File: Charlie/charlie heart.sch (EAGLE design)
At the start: 29 parts, among them Q1 BSA223SP

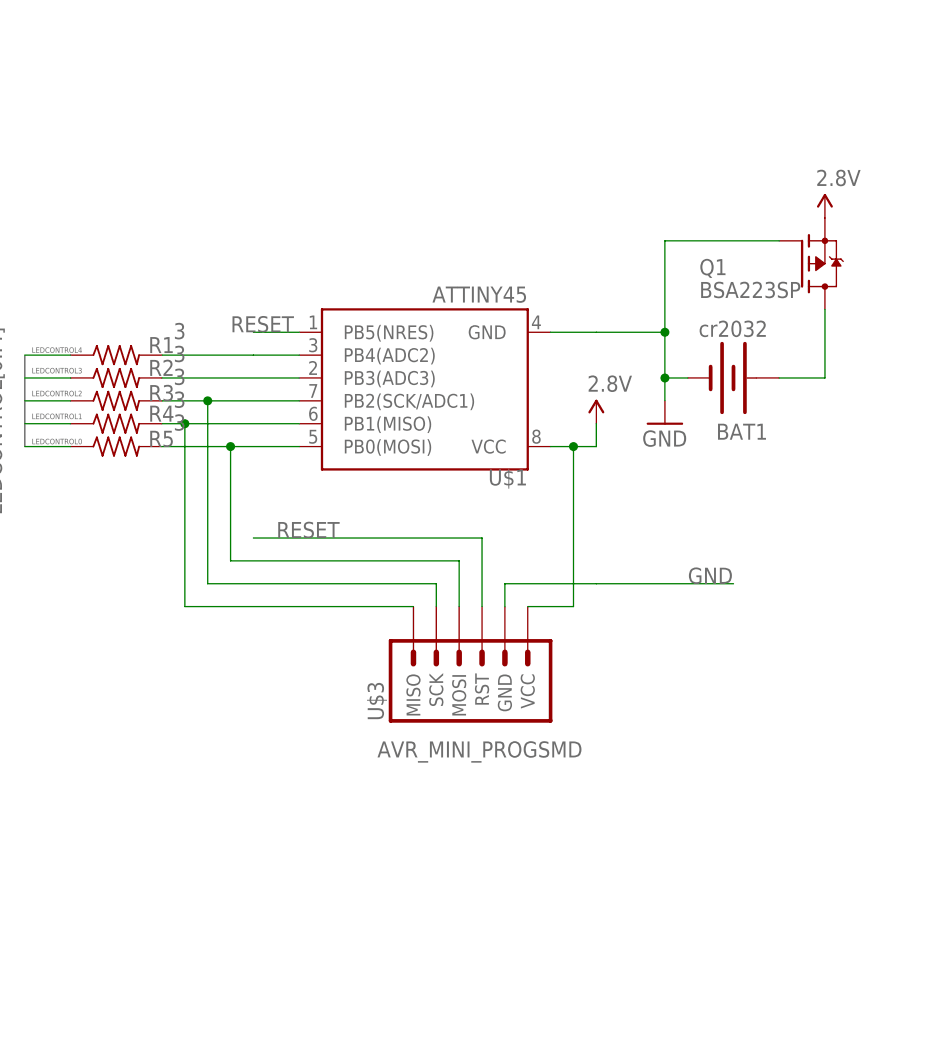
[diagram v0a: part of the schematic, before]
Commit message: add proper board file, and add mosfet for reverse battery safety
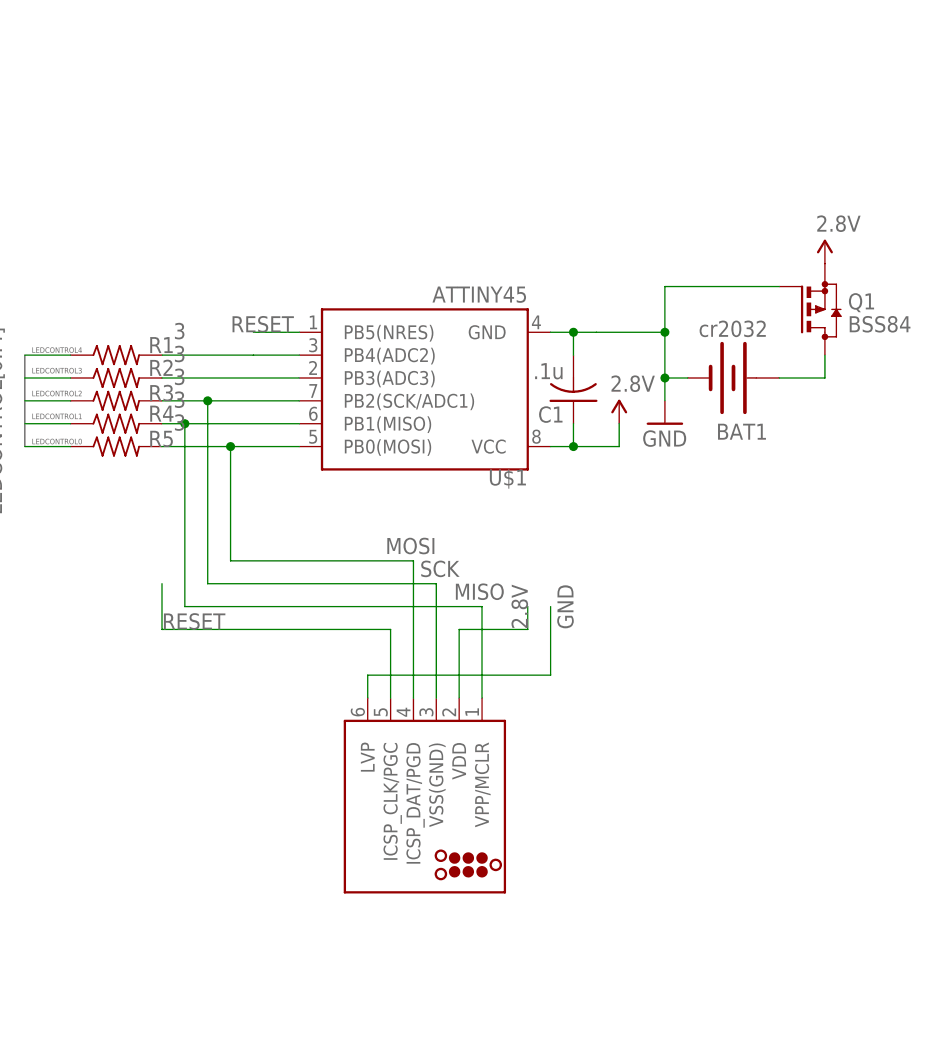
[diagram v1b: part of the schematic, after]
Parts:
- removed U$3: AVR_MINI_PROGSMD, SparkFun:AVR_MINI_PROGSMD
- added C1: .1u, rcl:C-USC1206
- added J1: (no value), tag-connect:TC2030-MCP-NL
- Q1: value BSA223SP -> BSS84; device transistor-fet:BSA223SP -> transistor-small-signal:BSS84
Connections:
- removed net N$1: R5.2, U$1.PB0(MOSI), U$3.MOSI
- removed net N$3: R3.2, U$1.PB2(SCK/ADC1), U$3.SCK
- removed net N$7: BAT1.+
- new net MISO: J1.VPP/MCLR, R4.2, U$1.PB1(MISO)
- new net MOSI: J1.ICSP_DAT/PGD, R5.2, U$1.PB0(MOSI)
- new net SCK: J1.VSS(GND), R3.2, U$1.PB2(SCK/ADC1)
- net 2.8V: now also C1.1, J1.VDD; no longer U$3.VCC
- net GND: now also C1.2, J1.LVP; no longer U$3.GND
- net N$2: now also BAT1.+, Q1.D; no longer R4.2, U$1.PB1(MISO), U$3.MISO
- net RESET: now also J1.ICSP_CLK/PGC; no longer U$3.RST
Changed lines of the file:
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@@
 <part name="BAT1" library="SparkFun" deviceset="BATTERY" device="20SMD" value="cr2032"/>
 <part name="GND1" library="SparkFun" deviceset="GND" device=""/>
-<part name="U$3" library="SparkFun" deviceset="AVR_MINI_PROG" device="SMD"/>
-<part name="Q1" library="transistor-fet" deviceset="BSA223SP" device=""/>
+<part name="C1" library="rcl" deviceset="C-US" device="C1206" value=".1u"/>
+<part name="J1" library="tag-connect" deviceset="TC2030" device="-MCP-NL"/>
+<part name="Q1" library="transistor-small-signal" deviceset="BSS84" device=""/>
 <part name="SUPPLY1" library="SparkFun-Aesthetics" deviceset="2.8V" device=""/>
 <part name="SUPPLY2" library="SparkFun-Aesthetics" deviceset="2.8V" device=""/>
@@
 <instance part="BAT1" gate="G$1" x="261.62" y="53.34" rot="R180"/>
 <instance part="GND1" gate="1" x="254" y="48.26"/>
-<instance part="U$3" gate="G$1" x="233.68" y="20.32" smashed="yes" rot="R270">
-<attribute name="NAME" x="222.758" y="15.24" size="1.778" layer="95" rot="R90"/>
-<attribute name="VALUE" x="244.856" y="12.954" size="1.778" layer="96" rot="R180"/>
-</instance>
-<instance part="Q1" gate="G$1" x="269.24" y="66.04"/>
-<instance part="SUPPLY1" gate="G$1" x="271.78" y="71.12"/>
-<instance part="SUPPLY2" gate="G$1" x="246.38" y="48.26"/>
+<instance part="C1" gate="G$1" x="243.84" y="50.8" rot="R180"/>
+<instance part="J1" gate="G$1" x="226.06" y="5.08" rot="R270"/>
+<instance part="Q1" gate="G$1" x="271.78" y="60.96"/>
+<instance part="SUPPLY1" gate="G$1" x="271.78" y="66.04"/>
+<instance part="SUPPLY2" gate="G$1" x="248.92" y="48.26"/>
 </instances>
 <busses>
@@
 </segment>
 </net>
-<net name="N$1" class="0">
+<net name="MOSI" class="0">
 <segment>
 <wire x1="213.36" y1="45.72" x2="205.74" y2="45.72" width="0.1524" layer="91"/>
 <wire x1="205.74" y1="45.72" x2="198.12" y2="45.72" width="0.1524" layer="91"/>
-<wire x1="231.14" y1="27.94" x2="231.14" y2="33.02" width="0.1524" layer="91"/>
-<wire x1="231.14" y1="33.02" x2="205.74" y2="33.02" width="0.1524" layer="91"/>
 <wire x1="205.74" y1="33.02" x2="205.74" y2="45.72" width="0.1524" layer="91"/>
 <junction x="205.74" y="45.72"/>
 <pinref part="U$1" gate="G$1" pin="PB0(MOSI)"/>
 <pinref part="R5" gate="G$1" pin="2"/>
-<pinref part="U$3" gate="G$1" pin="MOSI"/>
-</segment>
-</net>
-<net name="N$2" class="0">
+<pinref part="J1" gate="G$1" pin="ICSP_DAT/PGD"/>
+<wire x1="226.06" y1="17.78" x2="226.06" y2="33.02" width="0.1524" layer="91"/>
+<wire x1="226.06" y1="33.02" x2="205.74" y2="33.02" width="0.1524" layer="91"/>
+<label x="228.6" y="35.56" size="1.778" layer="95" rot="R180"/>
+</segment>
+</net>
+<net name="MISO" class="0">
 <segment>
 <wire x1="213.36" y1="48.26" x2="200.66" y2="48.26" width="0.1524" layer="91"/>
 <wire x1="200.66" y1="48.26" x2="198.12" y2="48.26" width="0.1524" layer="91"/>
-<wire x1="226.06" y1="27.94" x2="200.66" y2="27.94" width="0.1524" layer="91"/>
 <wire x1="200.66" y1="27.94" x2="200.66" y2="48.26" width="0.1524" layer="91"/>
 <junction x="200.66" y="48.26"/>
 <pinref part="U$1" gate="G$1" pin="PB1(MISO)"/>
 <pinref part="R4" gate="G$1" pin="2"/>
-<pinref part="U$3" gate="G$1" pin="MISO"/>
-</segment>
-</net>
-<net name="N$3" class="0">
+<pinref part="J1" gate="G$1" pin="VPP/MCLR"/>
+<wire x1="233.68" y1="17.78" x2="233.68" y2="27.94" width="0.1524" layer="91"/>
+<wire x1="233.68" y1="27.94" x2="200.66" y2="27.94" width="0.1524" layer="91"/>
+<label x="236.22" y="30.48" size="1.778" layer="95" rot="R180"/>
+</segment>
+</net>
+<net name="SCK" class="0">
 <segment>
 <wire x1="213.36" y1="50.8" x2="203.2" y2="50.8" width="0.1524" layer="91"/>
 <wire x1="203.2" y1="50.8" x2="198.12" y2="50.8" width="0.1524" layer="91"/>
-<wire x1="228.6" y1="27.94" x2="228.6" y2="30.48" width="0.1524" layer="91"/>
-<wire x1="228.6" y1="30.48" x2="203.2" y2="30.48" width="0.1524" layer="91"/>
 <wire x1="203.2" y1="30.48" x2="203.2" y2="50.8" width="0.1524" layer="91"/>
 <junction x="203.2" y="50.8"/>
 <pinref part="U$1" gate="G$1" pin="PB2(SCK/ADC1)"/>
 <pinref part="R3" gate="G$1" pin="2"/>
-<pinref part="U$3" gate="G$1" pin="SCK"/>
+<pinref part="J1" gate="G$1" pin="VSS(GND)"/>
+<wire x1="228.6" y1="17.78" x2="228.6" y2="30.48" width="0.1524" layer="91"/>
+<wire x1="228.6" y1="30.48" x2="203.2" y2="30.48" width="0.1524" layer="91"/>
+<label x="231.14" y="33.02" size="1.778" layer="95" rot="R180"/>
 </segment>
 </net>
@@
 <wire x1="256.54" y1="53.34" x2="254" y2="53.34" width="0.1524" layer="91"/>
 <wire x1="254" y1="53.34" x2="254" y2="50.8" width="0.1524" layer="91"/>
-<wire x1="241.3" y1="58.42" x2="246.38" y2="58.42" width="0.1524" layer="91"/>
+<wire x1="241.3" y1="58.42" x2="243.84" y2="58.42" width="0.1524" layer="91"/>
+<wire x1="243.84" y1="58.42" x2="246.38" y2="58.42" width="0.1524" layer="91"/>
 <wire x1="246.38" y1="58.42" x2="254" y2="58.42" width="0.1524" layer="91"/>
 <wire x1="254" y1="58.42" x2="254" y2="53.34" width="0.1524" layer="91"/>
@@
 <pinref part="GND1" gate="1" pin="GND"/>
 <pinref part="U$1" gate="G$1" pin="GND"/>
+<pinref part="C1" gate="G$1" pin="2"/>
+<wire x1="243.84" y1="55.88" x2="243.84" y2="58.42" width="0.1524" layer="91"/>
+<junction x="243.84" y="58.42"/>
 <pinref part="Q1" gate="G$1" pin="G"/>
-<wire x1="266.7" y1="68.58" x2="254" y2="68.58" width="0.1524" layer="91"/>
-<wire x1="254" y1="68.58" x2="254" y2="58.42" width="0.1524" layer="91"/>
+<wire x1="266.7" y1="63.5" x2="254" y2="63.5" width="0.1524" layer="91"/>
+<wire x1="254" y1="63.5" x2="254" y2="58.42" width="0.1524" layer="91"/>
 <junction x="254" y="58.42"/>
 </segment>
 <segment>
-<wire x1="261.62" y1="30.48" x2="246.38" y2="30.48" width="0.1524" layer="91"/>
-<wire x1="246.38" y1="30.48" x2="236.22" y2="30.48" width="0.1524" layer="91"/>
-<wire x1="236.22" y1="30.48" x2="236.22" y2="27.94" width="0.1524" layer="91"/>
-<pinref part="U$3" gate="G$1" pin="GND"/>
-<label x="256.54" y="30.48" size="1.778" layer="95"/>
+<pinref part="J1" gate="G$1" pin="LVP"/>
+<wire x1="220.98" y1="17.78" x2="220.98" y2="20.32" width="0.1524" layer="91"/>
+<wire x1="220.98" y1="20.32" x2="241.3" y2="20.32" width="0.1524" layer="91"/>
+<wire x1="241.3" y1="20.32" x2="241.3" y2="27.94" width="0.1524" layer="91"/>
+<label x="243.84" y="25.4" size="1.778" layer="95" rot="R90"/>
+</segment>
+</net>
+<net name="2.8V" class="0">
+<segment>
+<pinref part="J1" gate="G$1" pin="VDD"/>
+<wire x1="231.14" y1="17.78" x2="231.14" y2="25.4" width="0.1524" layer="91"/>
+<wire x1="231.14" y1="25.4" x2="238.76" y2="25.4" width="0.1524" layer="91"/>
+<wire x1="238.76" y1="25.4" x2="238.76" y2="27.94" width="0.1524" layer="91"/>
+<label x="238.76" y="25.4" size="1.778" layer="95" rot="R90"/>
+</segment>
+<segment>
+<pinref part="Q1" gate="G$1" pin="S"/>
+<pinref part="SUPPLY1" gate="G$1" pin="2.8V"/>
+</segment>
+<segment>
+<pinref part="C1" gate="G$1" pin="1"/>
+<wire x1="243.84" y1="48.26" x2="243.84" y2="45.72" width="0.1524" layer="91"/>
+<wire x1="241.3" y1="45.72" x2="243.84" y2="45.72" width="0.1524" layer="91"/>
+<pinref part="U$1" gate="G$1" pin="VCC"/>
+<wire x1="243.84" y1="45.72" x2="248.92" y2="45.72" width="0.1524" layer="91"/>
+<wire x1="248.92" y1="45.72" x2="248.92" y2="48.26" width="0.1524" layer="91"/>
+<junction x="243.84" y="45.72"/>
+<pinref part="SUPPLY2" gate="G$1" pin="2.8V"/>
 </segment>
 </net>
@@
 </segment>
 <segment>
-<wire x1="233.68" y1="35.56" x2="208.28" y2="35.56" width="0.1524" layer="91"/>
-<wire x1="233.68" y1="27.94" x2="233.68" y2="35.56" width="0.1524" layer="91"/>
-<label x="210.82" y="35.56" size="1.778" layer="95"/>
-<pinref part="U$3" gate="G$1" pin="RST"/>
-</segment>
-</net>
-<net name="N$7" class="0">
-<segment>
-<wire x1="271.78" y1="53.34" x2="271.78" y2="60.96" width="0.1524" layer="91"/>
+<pinref part="J1" gate="G$1" pin="ICSP_CLK/PGC"/>
+<wire x1="223.52" y1="17.78" x2="223.52" y2="25.4" width="0.1524" layer="91"/>
+<wire x1="223.52" y1="25.4" x2="198.12" y2="25.4" width="0.1524" layer="91"/>
+<wire x1="198.12" y1="25.4" x2="198.12" y2="30.48" width="0.1524" layer="91"/>
+<label x="198.12" y="25.4" size="1.778" layer="95"/>
+</segment>
+</net>
+<net name="N$2" class="0">
+<segment>
 <wire x1="266.7" y1="53.34" x2="271.78" y2="53.34" width="0.1524" layer="91"/>
 <pinref part="BAT1" gate="G$1" pin="+"/>
-</segment>
-</net>
-<net name="2.8V" class="0">
-<segment>
-<pinref part="Q1" gate="G$1" pin="S"/>
-<pinref part="SUPPLY1" gate="G$1" pin="2.8V"/>
-</segment>
-<segment>
-<wire x1="241.3" y1="45.72" x2="243.84" y2="45.72" width="0.1524" layer="91"/>
-<wire x1="243.84" y1="45.72" x2="243.84" y2="27.94" width="0.1524" layer="91"/>
-<wire x1="243.84" y1="27.94" x2="238.76" y2="27.94" width="0.1524" layer="91"/>
-<pinref part="U$1" gate="G$1" pin="VCC"/>
-<pinref part="U$3" gate="G$1" pin="VCC"/>
-<wire x1="243.84" y1="45.72" x2="246.38" y2="45.72" width="0.1524" layer="91"/>
-<wire x1="246.38" y1="45.72" x2="246.38" y2="48.26" width="0.1524" layer="91"/>
-<junction x="243.84" y="45.72"/>
-<pinref part="SUPPLY2" gate="G$1" pin="2.8V"/>
-</segment>
-</net>
+<pinref part="Q1" gate="G$1" pin="D"/>
+<wire x1="271.78" y1="53.34" x2="271.78" y2="55.88" width="0.1524" layer="91"/>
+</segment>
+</net>

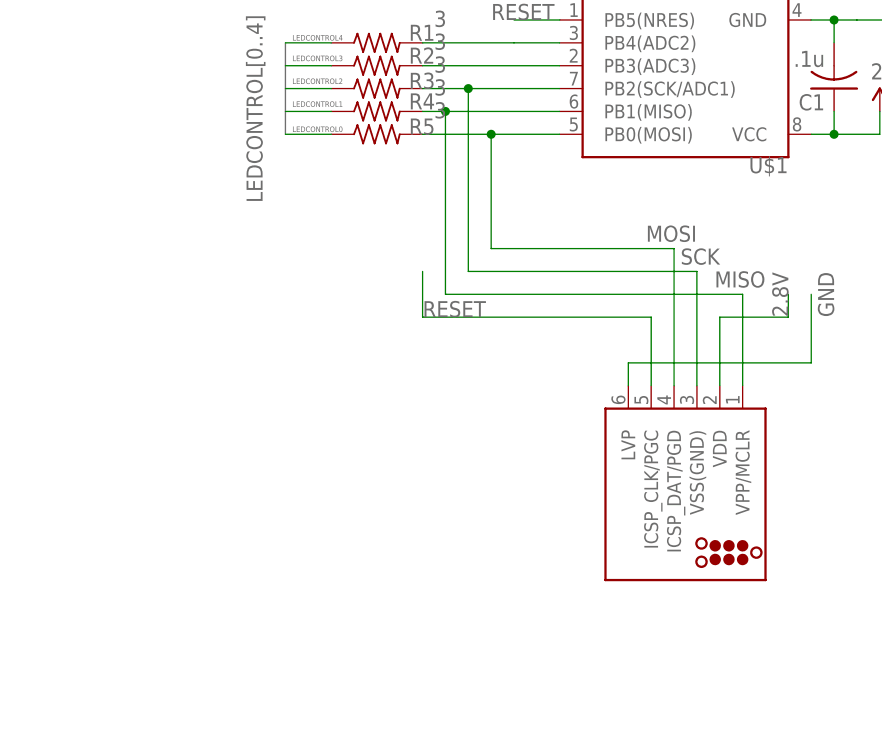
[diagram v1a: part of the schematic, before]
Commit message: add mode switch
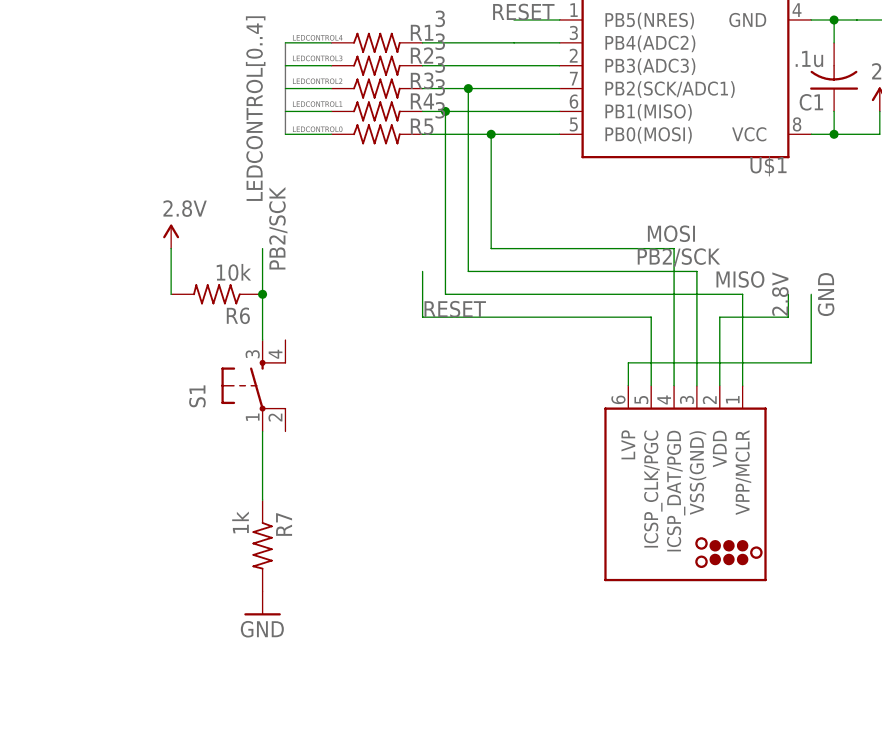
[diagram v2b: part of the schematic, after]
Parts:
- added R6: 10k, rcl:R-US_R0805
- added R7: 1k, rcl:R-US_R0805
- added S1: (no value), SparkFun:TAC_SWITCHSMD
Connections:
- removed net SCK: J1.VSS(GND), R3.2, U$1.PB2(SCK/ADC1)
- new net N$3: R7.1, S1.1
- new net PB2/SCK: J1.VSS(GND), R3.2, R6.1, S1.3, U$1.PB2(SCK/ADC1)
- net 2.8V: now also R6.2
- net GND: now also R7.2
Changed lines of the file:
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@@
 <part name="SUPPLY1" library="SparkFun-Aesthetics" deviceset="2.8V" device=""/>
 <part name="SUPPLY2" library="SparkFun-Aesthetics" deviceset="2.8V" device=""/>
+<part name="S1" library="SparkFun" deviceset="TAC_SWITCH" device="SMD"/>
+<part name="R6" library="rcl" deviceset="R-US_" device="R0805" value="10k"/>
+<part name="R7" library="rcl" deviceset="R-US_" device="R0805" value="1k"/>
+<part name="SUPPLY3" library="SparkFun-Aesthetics" deviceset="2.8V" device=""/>
+<part name="GND2" library="SparkFun-Aesthetics" deviceset="GND" device=""/>
 </parts>
 <sheets>
@@
 <instance part="SUPPLY1" gate="G$1" x="271.78" y="66.04"/>
 <instance part="SUPPLY2" gate="G$1" x="248.92" y="48.26"/>
+<instance part="S1" gate="S" x="180.34" y="17.78" rot="R90"/>
+<instance part="R6" gate="G$1" x="175.26" y="27.94" rot="R180"/>
+<instance part="R7" gate="G$1" x="180.34" y="0" rot="R270"/>
+<instance part="SUPPLY3" gate="G$1" x="170.18" y="33.02"/>
+<instance part="GND2" gate="1" x="180.34" y="-7.62"/>
 </instances>
 <busses>
@@
 </segment>
 </net>
-<net name="SCK" class="0">
+<net name="PB2/SCK" class="0">
 <segment>
 <wire x1="213.36" y1="50.8" x2="203.2" y2="50.8" width="0.1524" layer="91"/>
@@
 <wire x1="228.6" y1="30.48" x2="203.2" y2="30.48" width="0.1524" layer="91"/>
 <label x="231.14" y="33.02" size="1.778" layer="95" rot="R180"/>
+</segment>
+<segment>
+<pinref part="S1" gate="S" pin="3"/>
+<wire x1="180.34" y1="22.86" x2="180.34" y2="27.94" width="0.1524" layer="91"/>
+<pinref part="R6" gate="G$1" pin="1"/>
+<wire x1="180.34" y1="27.94" x2="180.34" y2="33.02" width="0.1524" layer="91"/>
+<junction x="180.34" y="27.94"/>
+<label x="182.88" y="30.48" size="1.778" layer="95" rot="R90"/>
 </segment>
 </net>
@@
 <label x="243.84" y="25.4" size="1.778" layer="95" rot="R90"/>
 </segment>
+<segment>
+<pinref part="R7" gate="G$1" pin="2"/>
+<pinref part="GND2" gate="1" pin="GND"/>
+</segment>
 </net>
 <net name="2.8V" class="0">
@@
 <pinref part="SUPPLY2" gate="G$1" pin="2.8V"/>
 </segment>
+<segment>
+<pinref part="R6" gate="G$1" pin="2"/>
+<wire x1="170.18" y1="27.94" x2="170.18" y2="33.02" width="0.1524" layer="91"/>
+<pinref part="SUPPLY3" gate="G$1" pin="2.8V"/>
+</segment>
 </net>
 <net name="RESET" class="0">
@@
 </segment>
 </net>
+<net name="N$3" class="0">
+<segment>
+<pinref part="S1" gate="S" pin="1"/>
+<wire x1="180.34" y1="12.7" x2="180.34" y2="5.08" width="0.1524" layer="91"/>
+<pinref part="R7" gate="G$1" pin="1"/>
+</segment>
+</net>
